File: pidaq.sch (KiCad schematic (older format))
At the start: 42 parts, among them J1 Screw_Terminal_01x08, J2 Screw_Terminal_01x08, J3 Screw_Terminal_01x10, J4 Screw_Terminal_01x10, J5 Conn_01x03_Male, J6 Conn_01x08_Female, U1 LTC2984CLX-DNP, U2 LTC2418IGN-DNP, U3 SN74LV1T34DCKR

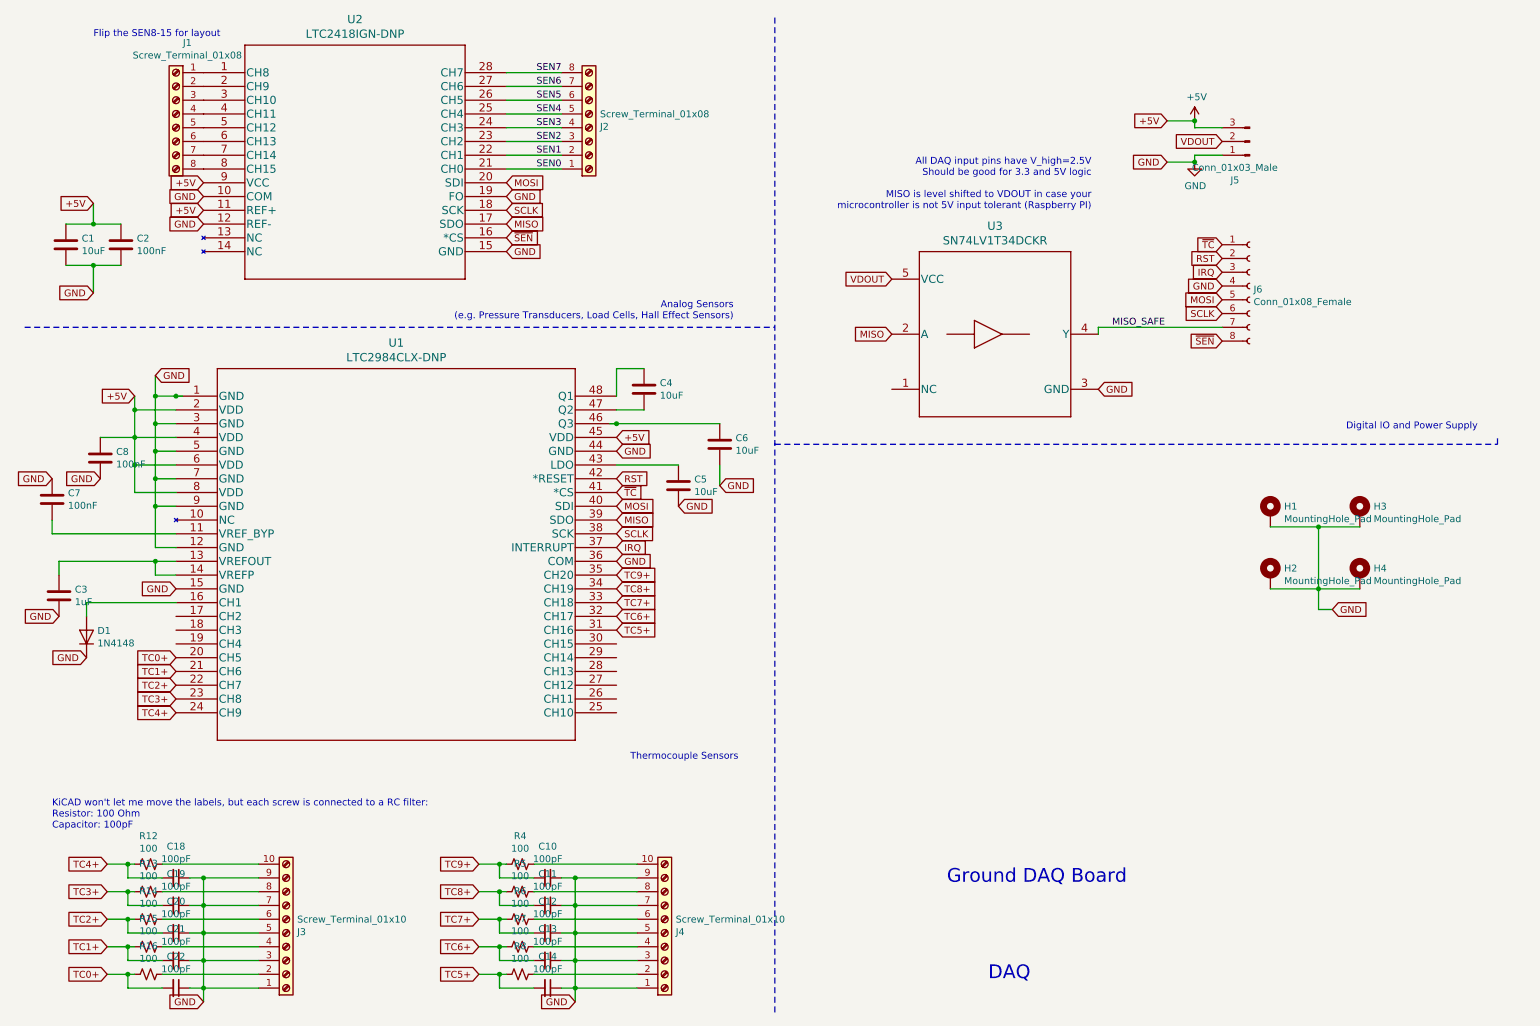
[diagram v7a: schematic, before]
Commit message: updated ics and load cell amplifier
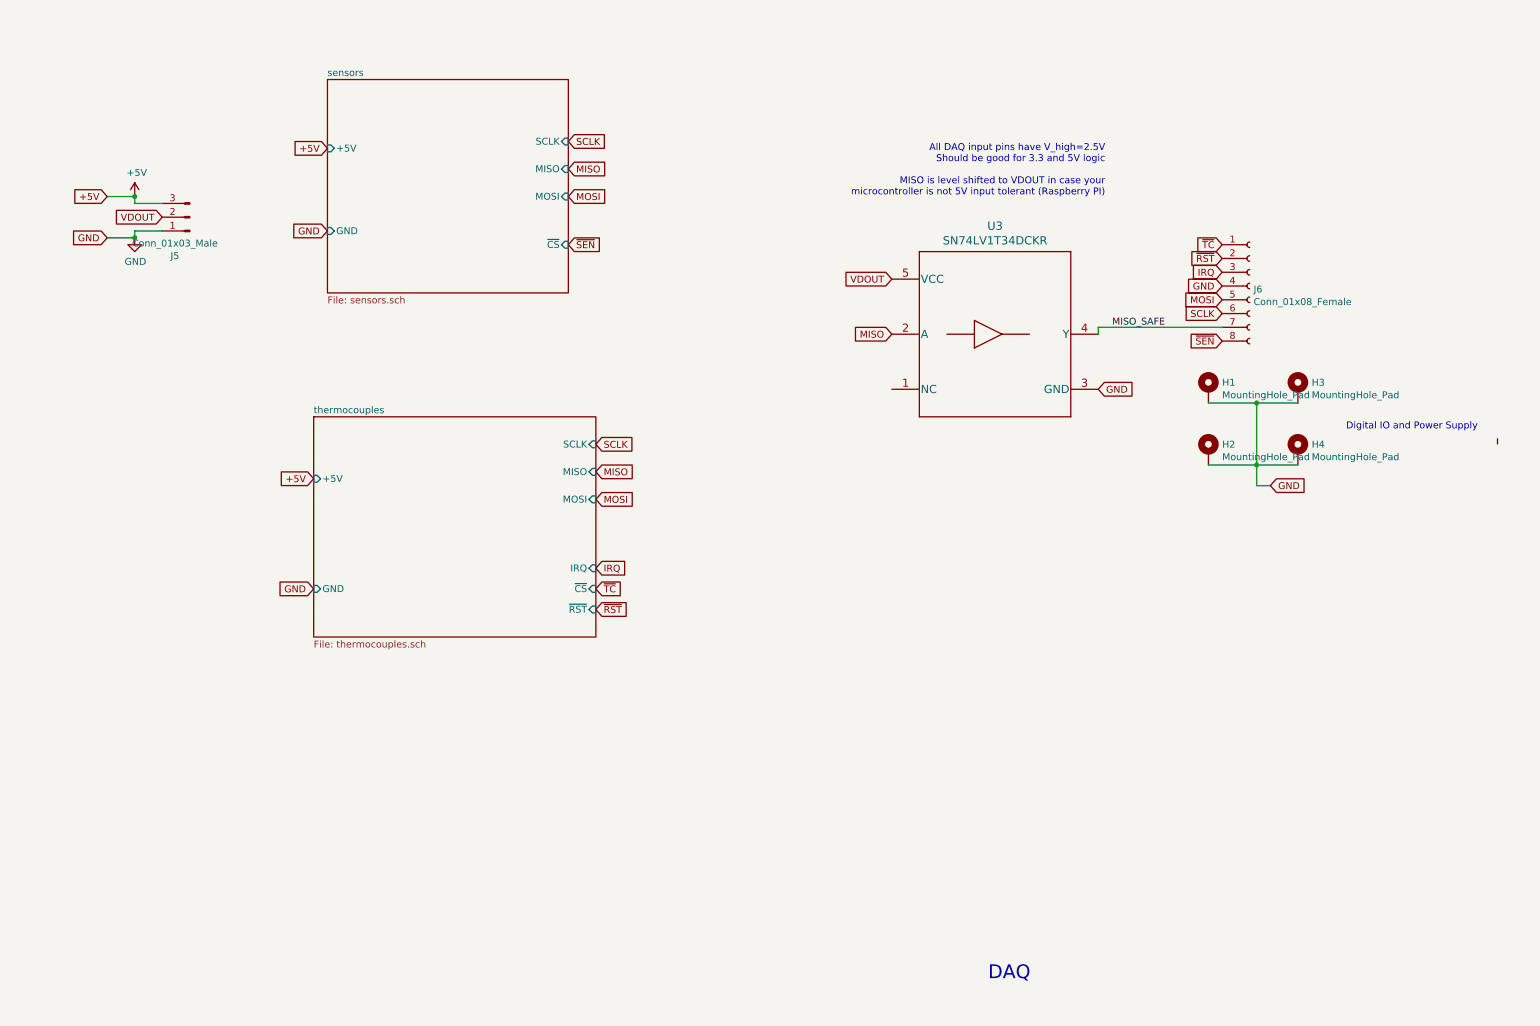
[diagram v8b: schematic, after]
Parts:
- removed C1, C4, C5, C6: 10uF, Capacitor_SMD:C_0805_2012Metric_Pad1.15x1.40mm_HandSolder, symbol Device:C
- removed C10, C11, C12, C13, C14, C18, C19, C20, C21, C22: 100pF, Capacitor_SMD:C_0805_2012Metric_Pad1.15x1.40mm_HandSolder, symbol Device:C_Small
- removed C2, C7, C8: 100nF, Capacitor_SMD:C_0805_2012Metric_Pad1.15x1.40mm_HandSolder, symbol Device:C
- removed C3: 1uF, Capacitor_SMD:C_0805_2012Metric_Pad1.15x1.40mm_HandSolder, symbol Device:C
- removed D1: 1N4148, Diode_THT:D_DO-35_SOD27_P7.62mm_Horizontal, symbol Diode:1N4148
- removed J1, J2: Screw_Terminal_01x08, TerminalBlock_Phoenix:TerminalBlock_Phoenix_MKDS-1,5-8-5.08_1x08_P5.08mm_Horizontal, symbol Connector:Screw_Terminal_01x08
- removed J3, J4: Screw_Terminal_01x10, TerminalBlock_Phoenix:TerminalBlock_Phoenix_PT-1,5-10-3.5-H_1x10_P3.50mm_Horizontal, symbol Connector:Screw_Terminal_01x10
- removed R12, R13, R14, R15, R16, R4, R5, R6, R7, R8: 100, Resistor_SMD:R_0805_2012Metric_Pad1.15x1.40mm_HandSolder, symbol Device:R_Small_US
- removed U1: LTC2984CLX-DNP, proj_footprints:LTC2984CLX-PBF, symbol LTC2984CLX:LTC2984CLX-PBF
- removed U2: LTC2418IGN-DNP, proj_footprints:LTC2418IGN-PBF, symbol LTC2418IGN:LTC2418IGN-PBF
- U3: footprint proj_footprints:SN74LV1T34DCKR -> footprints:SN74LV1T34DCKR
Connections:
- net RST renamed ~RST
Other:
- note removed: "Analog Sensors \n(e.g. Pressure Transducers, Load Cells, Hall Effect Sensors)"
- note removed: "Flip the SEN8-15 for layout"
- note removed: "Ground DAQ Board"
- note removed: "KiCAD won't let me move the labels, but each screw is connected to a RC filter:\nResistor: 100 Ohm\nCapacitor: 100pF"
- note removed: "Thermocouple Sensors\n"
- moved on the sheet: H1, H2, H3, H4, J5
